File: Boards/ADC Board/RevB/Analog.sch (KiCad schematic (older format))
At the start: 7 parts

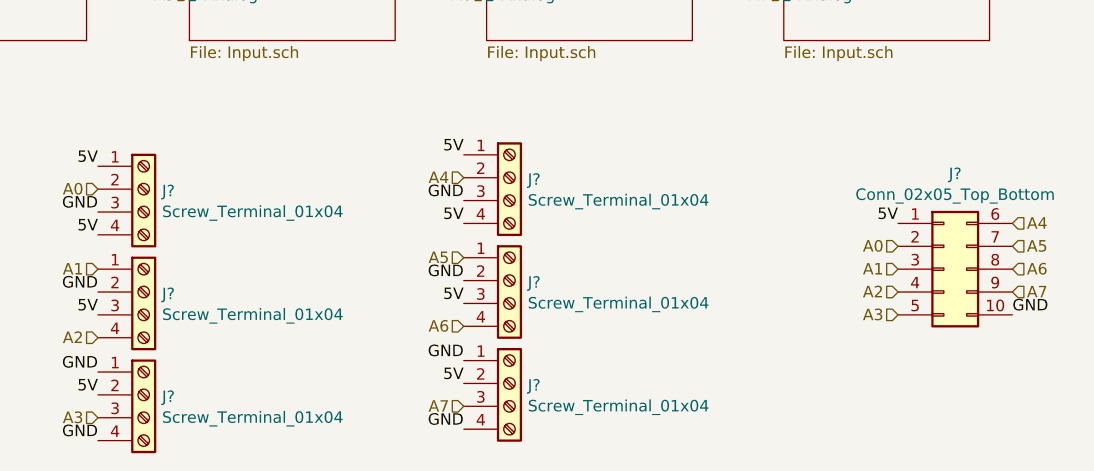
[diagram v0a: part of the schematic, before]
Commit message: Began footprint associations for rev b
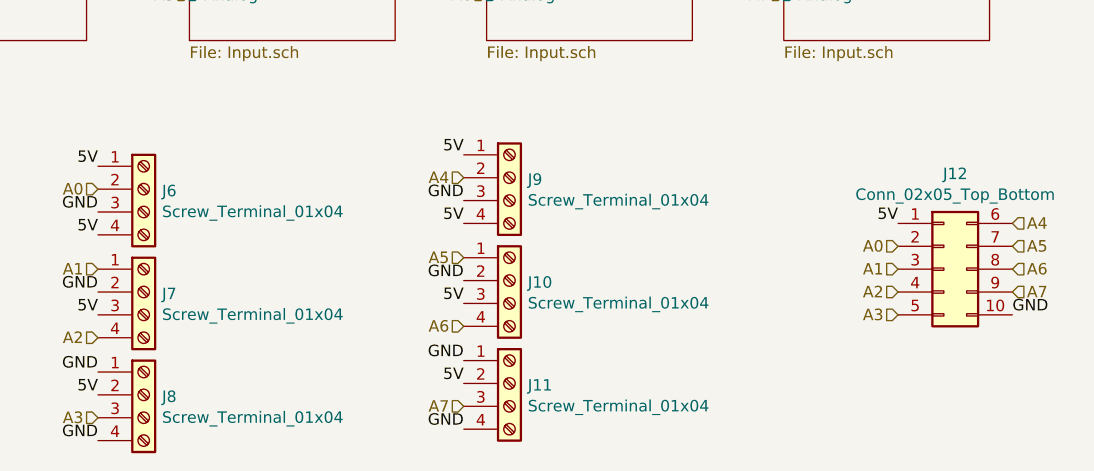
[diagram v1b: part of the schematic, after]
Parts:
- J10, J11, J6, J7, J8, J9: renamed from J?; footprint (none) -> Spring_Terminal_4Pin:1984989
- J12: renamed from J?; footprint (none) -> Connector_PinHeader_2.54mm:PinHeader_2x05_P2.54mm_Vertical
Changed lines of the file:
@@
 $Descr A4 11693 8268
 encoding utf-8
-Sheet 5 13
+Sheet 4 13
 Title ""
 Date ""
@@
 A6
 $Comp
-L Connector:Screw_Terminal_01x04 J?
+L Connector:Screw_Terminal_01x04 J6
 U 1 1 62338C0C
 P 2450 3900
-F 0 "J?" H 2530 3892 50  0000 L CNN
+F 0 "J6" H 2530 3892 50  0000 L CNN
 F 1 "Screw_Terminal_01x04" H 2530 3801 50  0000 L CNN
-F 2 "" H 2450 3900 50  0001 C CNN
+F 2 "Spring_Terminal_4Pin:1984989" H 2450 3900 50  0001 C CNN
 F 3 "~" H 2450 3900 50  0001 C CNN
 	1    2450 3900
@@
 $EndComp
 $Comp
-L Connector:Screw_Terminal_01x04 J?
+L Connector:Screw_Terminal_01x04 J8
 U 1 1 62339E59
 P 2450 4800
-F 0 "J?" H 2530 4792 50  0000 L CNN
+F 0 "J8" H 2530 4792 50  0000 L CNN
 F 1 "Screw_Terminal_01x04" H 2530 4701 50  0000 L CNN
-F 2 "" H 2450 4800 50  0001 C CNN
+F 2 "Spring_Terminal_4Pin:1984989" H 2450 4800 50  0001 C CNN
 F 3 "~" H 2450 4800 50  0001 C CNN
 	1    2450 4800
@@
 $EndComp
 $Comp
-L Connector:Screw_Terminal_01x04 J?
+L Connector:Screw_Terminal_01x04 J7
 U 1 1 6233ABB7
 P 2450 4350
-F 0 "J?" H 2530 4342 50  0000 L CNN
+F 0 "J7" H 2530 4342 50  0000 L CNN
 F 1 "Screw_Terminal_01x04" H 2530 4251 50  0000 L CNN
-F 2 "" H 2450 4350 50  0001 C CNN
+F 2 "Spring_Terminal_4Pin:1984989" H 2450 4350 50  0001 C CNN
 F 3 "~" H 2450 4350 50  0001 C CNN
 	1    2450 4350
@@
 $EndComp
 $Comp
-L Connector:Screw_Terminal_01x04 J?
+L Connector:Screw_Terminal_01x04 J9
 U 1 1 6234244F
 P 4050 3850
-F 0 "J?" H 4130 3842 50  0000 L CNN
+F 0 "J9" H 4130 3842 50  0000 L CNN
 F 1 "Screw_Terminal_01x04" H 4130 3751 50  0000 L CNN
-F 2 "" H 4050 3850 50  0001 C CNN
+F 2 "Spring_Terminal_4Pin:1984989" H 4050 3850 50  0001 C CNN
 F 3 "~" H 4050 3850 50  0001 C CNN
 	1    4050 3850
@@
 $EndComp
 $Comp
-L Connector:Screw_Terminal_01x04 J?
+L Connector:Screw_Terminal_01x04 J11
 U 1 1 62342455
 P 4050 4750
-F 0 "J?" H 4130 4742 50  0000 L CNN
+F 0 "J11" H 4130 4742 50  0000 L CNN
 F 1 "Screw_Terminal_01x04" H 4130 4651 50  0000 L CNN
-F 2 "" H 4050 4750 50  0001 C CNN
+F 2 "Spring_Terminal_4Pin:1984989" H 4050 4750 50  0001 C CNN
 F 3 "~" H 4050 4750 50  0001 C CNN
 	1    4050 4750
@@
 $EndComp
 $Comp
-L Connector:Screw_Terminal_01x04 J?
+L Connector:Screw_Terminal_01x04 J10
 U 1 1 6234245B
 P 4050 4300
-F 0 "J?" H 4130 4292 50  0000 L CNN
+F 0 "J10" H 4130 4292 50  0000 L CNN
 F 1 "Screw_Terminal_01x04" H 4130 4201 50  0000 L CNN
-F 2 "" H 4050 4300 50  0001 C CNN
+F 2 "Spring_Terminal_4Pin:1984989" H 4050 4300 50  0001 C CNN
 F 3 "~" H 4050 4300 50  0001 C CNN
 	1    4050 4300
@@
 A7
 $Comp
-L Connector_Generic:Conn_02x05_Top_Bottom J?
+L Connector_Generic:Conn_02x05_Top_Bottom J12
 U 1 1 623441A1
 P 5950 4250
-F 0 "J?" H 6000 4667 50  0000 C CNN
+F 0 "J12" H 6000 4667 50  0000 C CNN
 F 1 "Conn_02x05_Top_Bottom" H 6000 4576 50  0000 C CNN
-F 2 "" H 5950 4250 50  0001 C CNN
+F 2 "Connector_PinHeader_2.54mm:PinHeader_2x05_P2.54mm_Vertical" H 5950 4250 50  0001 C CNN
 F 3 "~" H 5950 4250 50  0001 C CNN
 	1    5950 4250
